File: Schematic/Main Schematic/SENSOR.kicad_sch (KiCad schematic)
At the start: 12 parts, among them IC2 LM75AD,118, J2 Conn_01x02_Pin

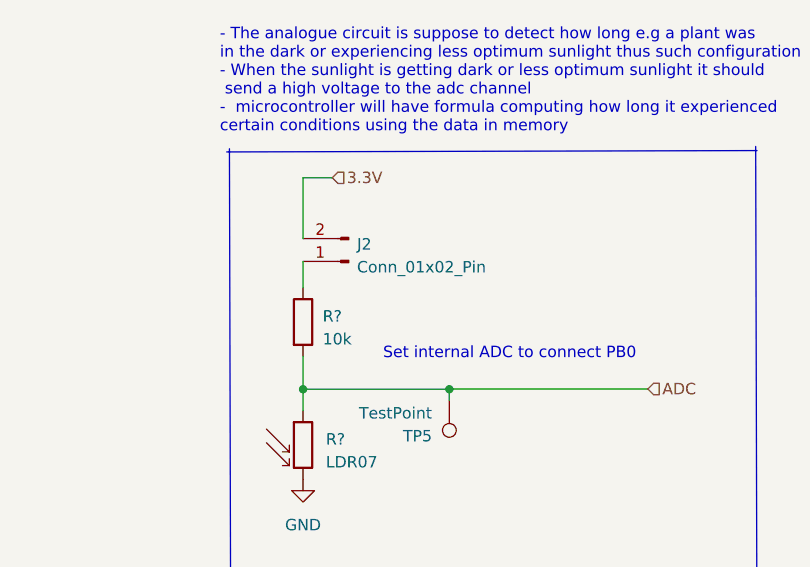
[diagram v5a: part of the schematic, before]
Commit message: corrected drc and unrouted issues
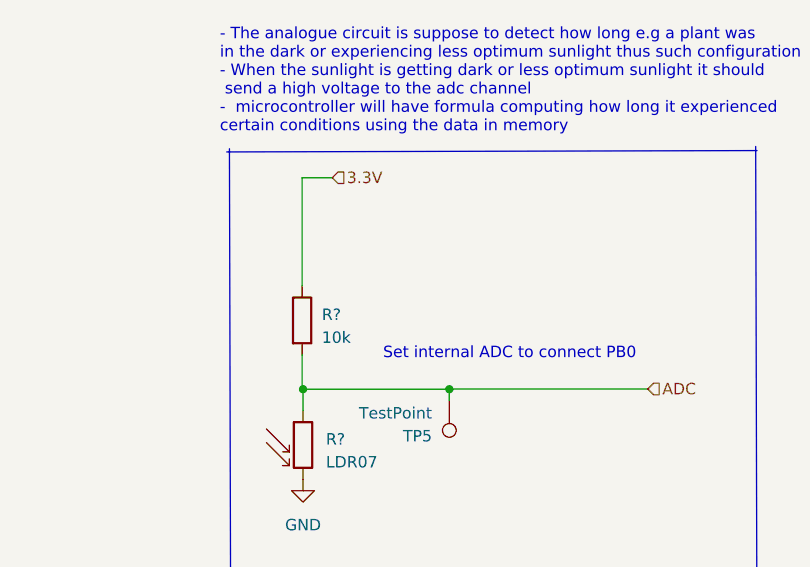
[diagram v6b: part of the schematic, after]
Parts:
- removed J2: Conn_01x02_Pin, Connector_PinHeader_2.54mm:PinHeader_1x02_P2.54mm_Vertical, symbol Connector:Conn_01x02_Pin
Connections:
- net 3.3V: now also R?.1
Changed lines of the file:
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@@
     (comment 4 "Author: Zwivhuya Ndou")
   )
+  (junction (at 71.9582 122.9106) (diameter 0) (color 0 0 0 0)
+  )
+  (junction (at 110.6932 125.4506) (diameter 0) (color 0 0 0 0)
+  )
+  (junction (at 113.2332 100.0506) (diameter 0) (color 0 0 0 0)
+  )
+  (junction (at 113.2332 105.7656) (diameter 0) (color 0 0 0 0)
+  )
+  (junction (at 78.9432 105.7656) (diameter 0) (color 0 0 0 0)
+  )
+  (junction (at 110.6932 127.9906) (diameter 0) (color 0 0 0 0)
+  )
+  (junction (at 82.1182 120.3706) (diameter 0) (color 0 0 0 0)
+  )
   (junction (at 164.1856 111.379) (diameter 0) (color 0 0 0 0)
   )
-  (junction (at 71.9582 122.9106) (diameter 0) (color 0 0 0 0)
-  )
-  (junction (at 110.6932 125.4506) (diameter 0) (color 0 0 0 0)
-  )
-  (junction (at 113.2332 100.0506) (diameter 0) (color 0 0 0 0)
-  )
-  (junction (at 113.2332 105.7656) (diameter 0) (color 0 0 0 0)
-  )
-  (junction (at 78.9432 105.7656) (diameter 0) (color 0 0 0 0)
-  )
-  (junction (at 110.6932 127.9906) (diameter 0) (color 0 0 0 0)
-  )
-  (junction (at 82.1182 120.3706) (diameter 0) (color 0 0 0 0)
-  )
   (junction (at 180.4416 111.379) (diameter 0) (color 0 0 0 0)
   )
@@
     (stroke (width 0) (type default))
   )
+  (wire (pts (xy 164.084 87.884) (xy 164.084 99.9236))
+    (stroke (width 0) (type default))
+  )
   (wire (pts (xy 70.0532 122.9106) (xy 70.0532 113.3856))
     (stroke (width 0) (type default))
@@
     (stroke (width 0) (type default))
   )
-  (wire (pts (xy 164.1856 107.7214) (xy 164.1856 111.379))
+  (wire (pts (xy 164.084 107.5436) (xy 164.084 111.379))
     (stroke (width 0) (type default))
   )
@@
     (stroke (width 0) (type default))
   )
-  (wire (pts (xy 164.1856 94.6404) (xy 164.1856 87.884))
-    (stroke (width 0) (type default))
-  )
   (wire (pts (xy 65.6082 125.4506) (xy 85.2932 125.4506))
     (stroke (width 0) (type default))
@@
     (stroke (width 0) (type default))
   )
+  (wire (pts (xy 164.084 111.379) (xy 164.1856 111.379))
+    (stroke (width 0) (type default))
+  )
   (polyline (pts (xy 57.3024 141.9606) (xy 57.2008 83.6422))
     (stroke (width 0) (type default))
@@
     (stroke (width 0) (type default))
   )
-  (wire (pts (xy 164.1856 87.884) (xy 167.4368 87.884))
+  (wire (pts (xy 164.084 87.884) (xy 167.4368 87.884))
     (stroke (width 0) (type default))
   )
@@
   )
   (wire (pts (xy 78.9432 120.3706) (xy 78.9432 113.3856))
-    (stroke (width 0) (type default))
-  )
-  (wire (pts (xy 164.1856 97.1804) (xy 164.1856 100.1014))
     (stroke (width 0) (type default))
   )
@@
   (hierarchical_label "3.3V" (shape input) (at 113.1824 92.4052 0) (fields_autoplaced)
     (effects (font (size 1.27 1.27)) (justify left))
-  )
-  (symbol (lib_id "Connector:Conn_01x02_Pin") (at 169.2656 97.1804 180) (unit 1)
-    (in_bom yes) (on_board yes) (dnp no) (fields_autoplaced)
-    (property "Reference" "J2" (at 170.18 95.2754 0)
-      (effects (font (size 1.27 1.27)) (justify right))
-    )
-    (property "Value" "Conn_01x02_Pin" (at 170.18 97.8154 0)
-      (effects (font (size 1.27 1.27)) (justify right))
-    )
-    (property "Footprint" "Connector_PinHeader_2.54mm:PinHeader_1x02_P2.54mm_Vertical" (at 169.2656 97.1804 0)
-      (effects (font (size 1.27 1.27)) hide)
-    )
-    (property "Datasheet" "~" (at 169.2656 97.1804 0)
-      (effects (font (size 1.27 1.27)) hide)
-    )
-    (pin "1")
-    (pin "2")
-    (instances
-      (project "Main Schematic"
-        (path "/81c41bad-bb43-41af-b405-18d135a809b1/820a1ce6-42c1-4792-8ad0-5e2a5c074ed4"
-          (reference "J2") (unit 1)
-        )
-      )
-    )
   )
   (symbol (lib_id "power:GND") (at 110.6932 129.2606 0) (unit 1)
@@
     )
   )
-  (symbol (lib_id "Device:R") (at 164.1856 103.9114 0) (unit 1)
-    (in_bom yes) (on_board yes) (dnp no) (fields_autoplaced)
-    (property "Reference" "R?" (at 166.37 103.2764 0)
-      (effects (font (size 1.27 1.27)) (justify left))
-    )
-    (property "Value" "10k" (at 166.37 105.8164 0)
-      (effects (font (size 1.27 1.27)) (justify left))
-    )
-    (property "Footprint" "Local_Footprints:R0805" (at 162.4076 103.9114 90)
-      (effects (font (size 1.27 1.27)) hide)
-    )
-    (property "Datasheet" "~" (at 164.1856 103.9114 0)
-      (effects (font (size 1.27 1.27)) hide)
-    )
+  (symbol (lib_id "Device:R") (at 164.084 103.7336 0) (unit 1)
+    (in_bom yes) (on_board yes) (dnp no) (fields_autoplaced)
+    (property "Reference" "R?" (at 166.2684 103.0986 0)
+      (effects (font (size 1.27 1.27)) (justify left))
+    )
+    (property "Value" "10k" (at 166.2684 105.6386 0)
+      (effects (font (size 1.27 1.27)) (justify left))
+    )
+    (property "Footprint" "Local_Footprints:R0805" (at 162.306 103.7336 90)
+      (effects (font (size 1.27 1.27)) hide)
+    )
+    (property "Datasheet" "~" (at 164.084 103.7336 0)
+      (effects (font (size 1.27 1.27)) hide)
+    )

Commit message: pcb files all in order and showing perfect on jlcpcb
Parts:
- R?: footprint Local_Footprints:R0805 -> Resistor_SMD:R_0805_2012Metric
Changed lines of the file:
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@@
       (effects (font (size 1.27 1.27)) (justify left))
     )
-    (property "Footprint" "Local_Footprints:R0805" (at 162.306 103.7336 90)
+    (property "Footprint" "Resistor_SMD:R_0805_2012Metric" (at 162.306 103.7336 90)
       (effects (font (size 1.27 1.27)) hide)
     )
